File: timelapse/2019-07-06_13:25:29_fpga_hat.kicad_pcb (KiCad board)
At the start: 4 copper layers, 65 x 56.5 mm, 92 parts, among them J1 2x20, J2 AudioJack3, J3 Conn_02x06_Top_Bottom, J4 Conn_02x06_Top_Bottom, J5 Conn_02x06_Top_Bottom, J6 Conn_01x02, SW1 PTS815, SW2 PTS815, SW3 PTS815, SW4 PTS815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

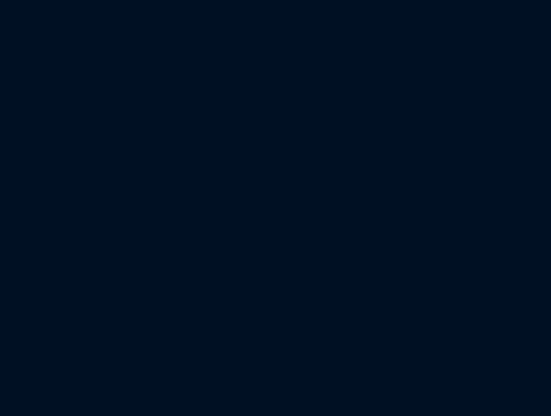
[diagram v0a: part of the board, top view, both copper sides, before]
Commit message: Tidy up both silkscreen layers. Remove copper from mounting hole screw lands.
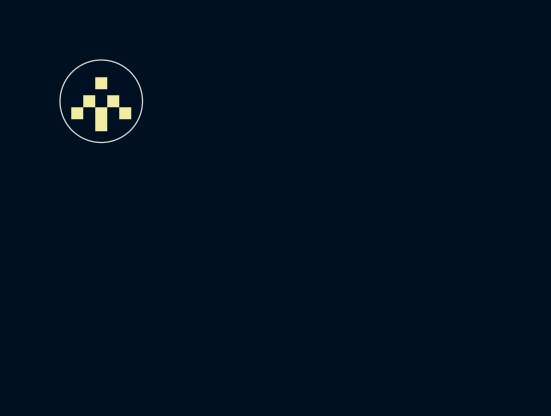
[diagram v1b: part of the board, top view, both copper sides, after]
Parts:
- added REF**: MOUNTHOLE_M2.5, fpga_hat:MOUNTHOLE_M2.5, F.Cu at (0.00, 0.00)
- added REF**: github_avatar, fpga_hat:github_avatar, F.Cu at (0.00, 0.00)
